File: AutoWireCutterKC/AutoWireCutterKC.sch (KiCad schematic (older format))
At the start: 20 parts, among them J1 LCD I/O, J2 ISP, J3 LCD Serial, J5 LCD Power, J6 Servo, J8 Barrel_Jack, J9 Stepper, M1 Conn_01x01_Male, M2 Conn_01x01_Male, M3 Conn_01x01_Male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

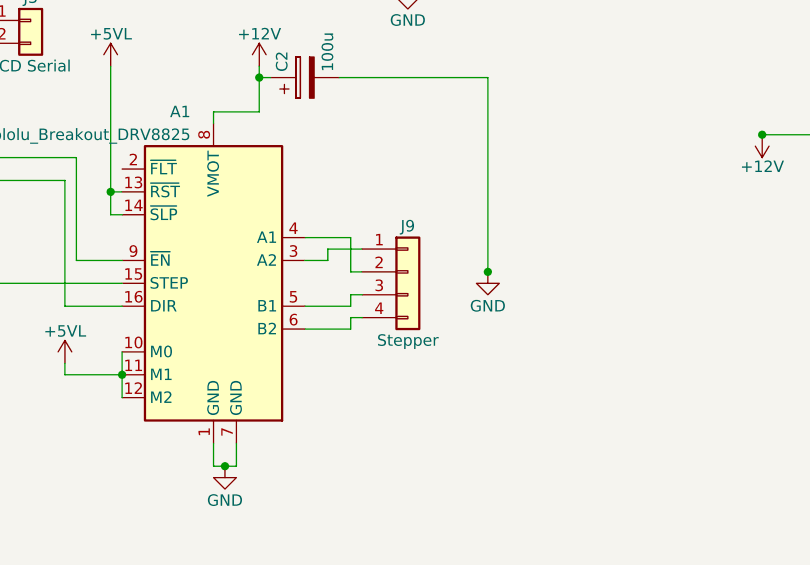
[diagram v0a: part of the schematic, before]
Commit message: Schematic Rev B
Moved silk screen, motor con through holes widened, motor connector fit on top.
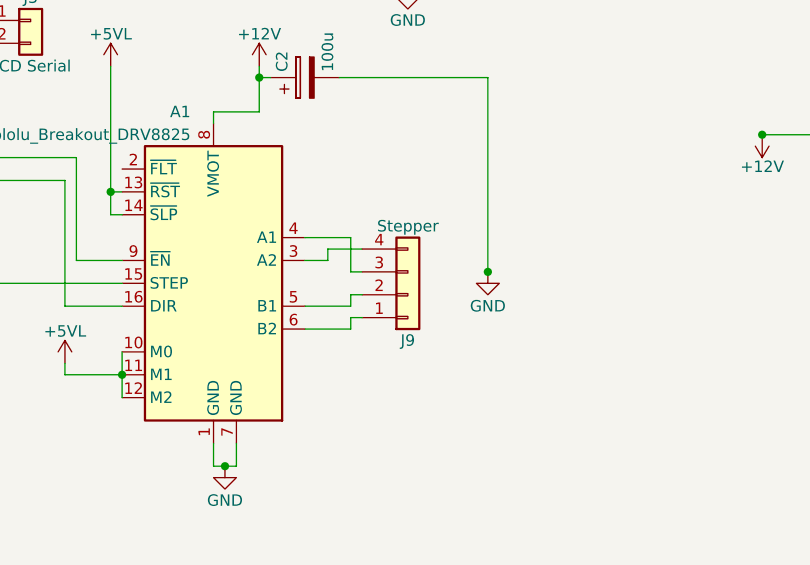
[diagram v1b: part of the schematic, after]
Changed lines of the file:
@@
 L Conn_01x04 J9
 U 1 1 5B1801EF
-P 6600 5050
-F 0 "J9" H 6600 5250 50  0000 C CNN
-F 1 "Stepper" H 6600 4750 50  0000 C CNN
-F 2 "Pin_Headers:Pin_Header_Straight_1x04_Pitch2.54mm" H 6600 5050 50  0001 C CNN
-F 3 "" H 6600 5050 50  0001 C CNN
-	1    6600 5050
-	1    0    0    -1
+P 6600 5150
+F 0 "J9" H 6600 5350 50  0000 C CNN
+F 1 "Stepper" H 6600 4850 50  0000 C CNN
+F 2 "Pin_Headers:Pin_Header_Straight_1x04_Pitch2.54mm" H 6600 5150 50  0001 C CNN
+F 3 "" H 6600 5150 50  0001 C CNN
+	1    6600 5150
+	1    0    0    1
 $EndComp
 $Comp

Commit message: Added Pinout for Keypad, Began schematic work for future boards
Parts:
- removed U2: MCP1700_SOT23, TO_SOT_Packages_SMD:SOT-23, symbol MCP1700-5002E_SOT23
- added U2: LM3480-5.0, TO_SOT_Packages_SMD:SOT-23, symbol LM3480-5.0
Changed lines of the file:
@@
-$EndComp
-$Comp
-L MCP1700-5002E_SOT23 U2
-U 1 1 5B1E96C1
-P 8950 4450
-F 0 "U2" H 8800 4575 50  0000 C CNN
-F 1 "MCP1700_SOT23" H 8950 4575 50  0000 L CNN
-F 2 "TO_SOT_Packages_SMD:SOT-23" H 8950 4675 50  0001 C CNN
-F 3 "" H 8950 4450 50  0001 C CNN
-	1    8950 4450
-	1    0    0    -1
 $EndComp
 $Comp
@@
 	9300 4500 9300 4450
 Wire Wire Line
-	9250 4450 9600 4450
-Wire Wire Line
 	8450 4500 8450 4450
-Wire Wire Line
-	8150 4450 8650 4450
 Wire Wire Line
 	9250 2400 9250 2700
@@
 	6000 4200 5950 4200
 Connection ~ 5950 4200
-Connection ~ 8650 4450
 Connection ~ 8150 4450
 Connection ~ 9600 4450
@@
 Connection ~ 9250 3650
 Connection ~ 8650 3650
-Connection ~ 8950 4750
 Connection ~ 8950 4850
 Connection ~ 6600 3800
@@
 $EndComp
 $Comp
-L GND #PWR?
+L GND #PWR021
 U 1 1 5B21B02C
 P 13700 2700
-F 0 "#PWR?" H 13700 2450 50  0001 C CNN
+F 0 "#PWR021" H 13700 2450 50  0001 C CNN
 F 1 "GND" H 13700 2550 50  0000 C CNN
 F 2 "" H 13700 2700 50  0001 C CNN
@@
 	13550 2950 13400 2950
 Connection ~ 13550 2700
+$Comp
+L LM3480-5.0 U2
+U 1 1 5B55ECDD
+P 8950 4450
+F 0 "U2" H 8800 4575 50  0000 C CNN
+F 1 "LM3480-5.0" H 8950 4575 50  0000 L CNN
+F 2 "TO_SOT_Packages_SMD:SOT-23" H 8950 4675 50  0001 C CIN
+F 3 "" H 8950 4450 50  0001 C CNN
+	1    8950 4450
+	1    0    0    -1
+$EndComp
+Wire Wire Line
+	8150 4450 8650 4450
+Wire Wire Line
+	9250 4450 9600 4450
 $EndSCHEMATC

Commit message: In Progress: Changing Schematic
Rev C
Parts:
- removed C3, C4: 1u, Capacitors_SMD:C_0805_HandSoldering, symbol C
- removed J3: LCD Serial, Pin_Headers:Pin_Header_Angled_1x02_Pitch2.54mm, symbol Conn_01x02
- removed U2: LM3480-5.0, TO_SOT_Packages_SMD:SOT-23, symbol LM3480-5.0
- added J3: TX, symbol Connector:Conn_01x01_Male
- added U2: CRE1S1205SC, Converter_DCDC:Converter_DCDC_muRata_CRE1xxxxxxSC_THT, symbol Regulator_Switching:CRE1S1205SC
- A1: symbol Pololu_Breakout_DRV8825 -> Driver_Motor:Pololu_Breakout_DRV8825
- C1, C5: symbol C -> Device:C
- C2: symbol CP -> Device:CP
- C6: symbol CP1 -> Device:CP1
- J1: symbol Conn_01x08 -> AutoWireCutterKC-rescue:Conn_01x08
- J2: symbol Conn_02x03_Odd_Even -> AutoWireCutterKC-rescue:Conn_02x03_Odd_Even
- J5: symbol Conn_01x02 -> AutoWireCutterKC-rescue:Conn_01x02
- J6: symbol Conn_01x03 -> AutoWireCutterKC-rescue:Conn_01x03
- J8: symbol Barrel_Jack -> AutoWireCutterKC-rescue:Barrel_Jack
- J9: symbol Conn_01x04 -> AutoWireCutterKC-rescue:Conn_01x04
- M1, M2, M3: symbol Conn_01x01_Male -> AutoWireCutterKC-rescue:Conn_01x01_Male
- U1: symbol ATMEGA328P-AU -> AutoWireCutterKC-rescue:ATMEGA328P-AU
- U3: symbol LT1129-5.0_SOT223 -> AutoWireCutterKC-rescue:LT1129-5.0_SOT223
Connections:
- net labels added: GNDREF
- wire segments 122 -> 139
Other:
- moved on the sheet: M1, M2, M3

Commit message: Board RevC
Added DC-to-DC converter for isolation, LED for status indication, increased board size and mounting holes and changed pin allocations for more efficient programming.
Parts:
- removed J3: TX, symbol Connector:Conn_01x01_Male
- removed J5: LCD Power, Pin_Headers:Pin_Header_Angled_1x02_Pitch2.54mm, symbol AutoWireCutterKC-rescue:Conn_01x02
- added D1: LED, LEDs:LED_0805_HandSoldering, symbol Device:LED
- added I1: NSI50010YT1G, Diodes_SMD:D_SOD-123, symbol DanaCustom:NSI50010YT1G
- added J3: LCD, Pin_Headers:Pin_Header_Angled_1x03_Pitch2.54mm, symbol Connector:Conn_01x03_Male
- added M4: Conn_01x01_Male, Mounting_Holes:MountingHole_3.2mm_M3_ISO7380_Pad, symbol AutoWireCutterKC-rescue:Conn_01x01_Male
- A1: footprint Module:Pololu_Breakout-16_15.2x20.3mm -> Modules:Pololu_Breakout-16_15.2x20.3mm
- J9: footprint Pin_Headers:Pin_Header_Straight_1x04_Pitch2.54mm -> DanaCustomLibrary:JST_PH_B4B_StressReliefCorrect
- M1, M2, M3: footprint (none) -> Mounting_Holes:MountingHole_3.2mm_M3_ISO7380_Pad
- U2: footprint Converter_DCDC:Converter_DCDC_muRata_CRE1xxxxxxSC_THT -> DanaCustomLibrary:CRE1S1205SC_DC_to_DC
- renumbered J6 to J5
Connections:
- net labels added: Mounting_Holes
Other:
- moved on the sheet: C5, C6, J5, J8, M1, M2, M3, U2, U3
